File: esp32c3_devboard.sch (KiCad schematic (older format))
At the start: 0 parts

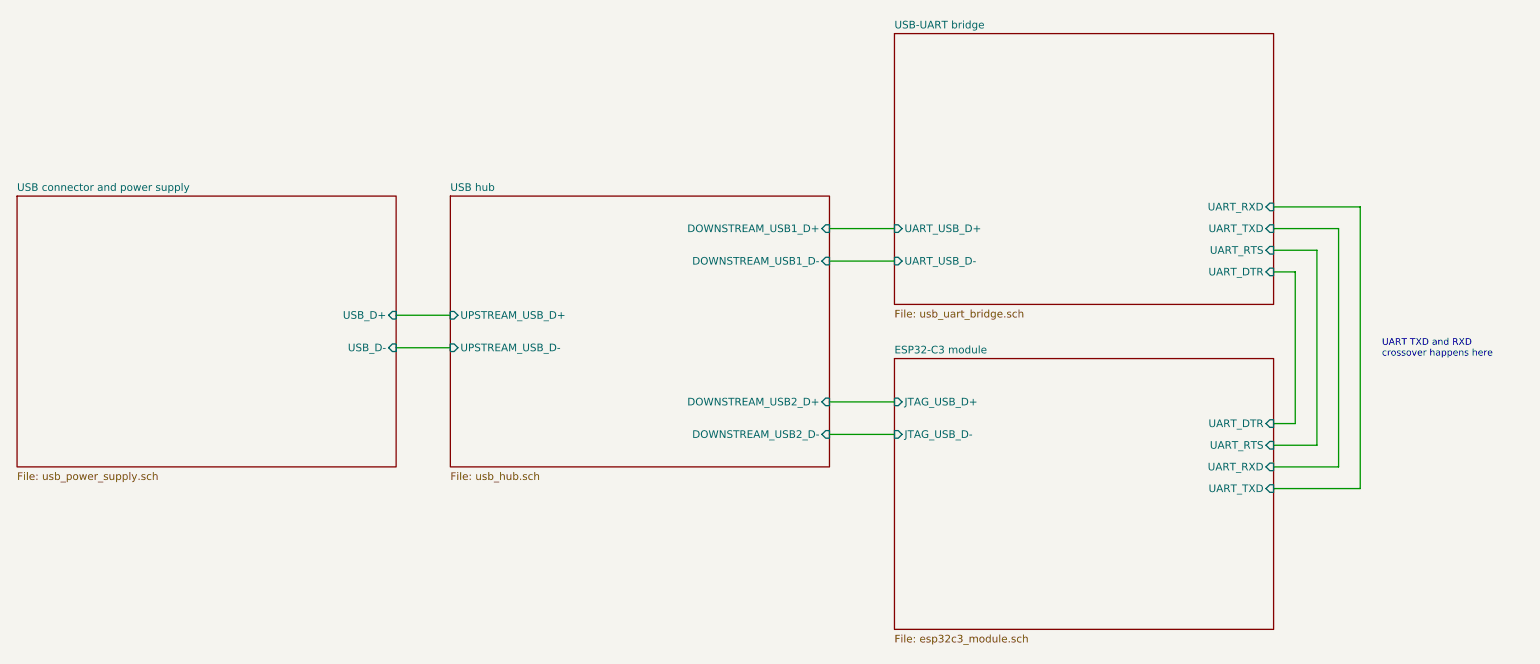
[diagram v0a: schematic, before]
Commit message: Use ESP32-C3-WROOM-02 module
Signed-off-by: Tomislav Milkovic <tomislav.milkovic95@gmail.com>
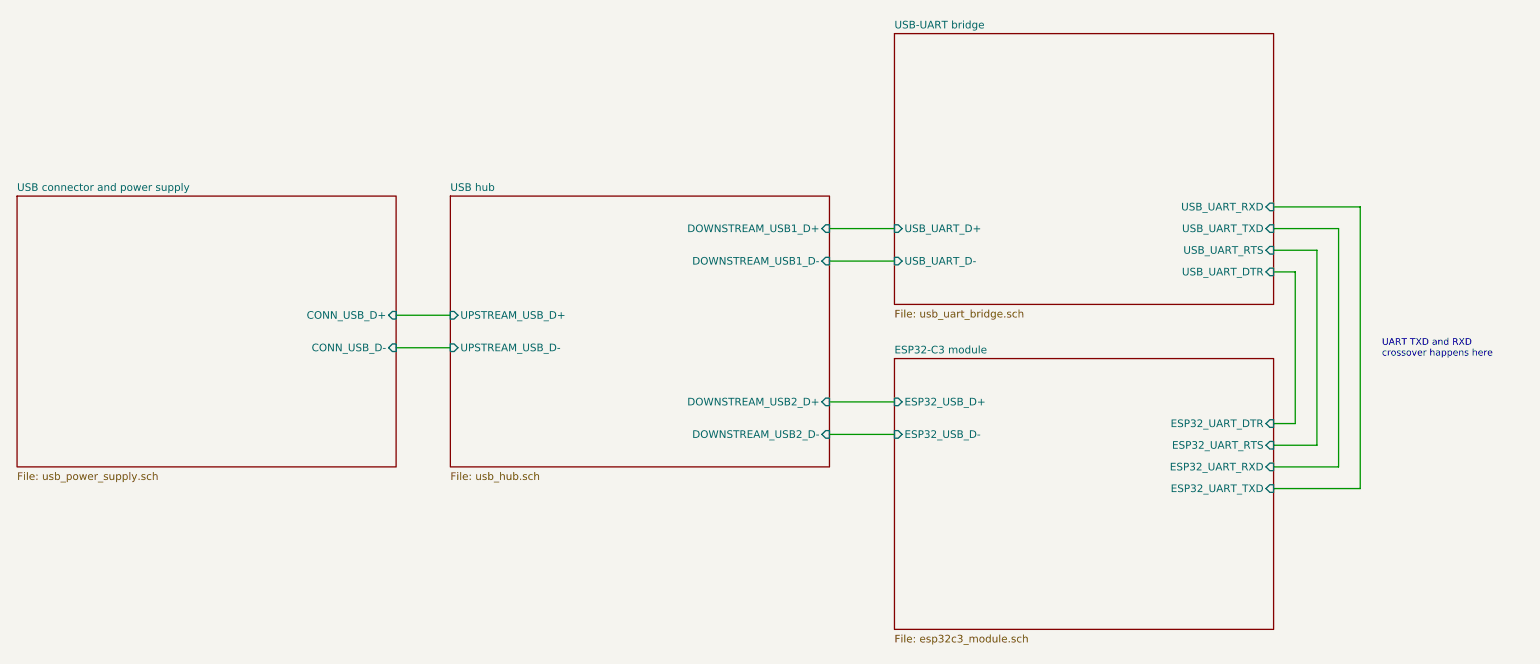
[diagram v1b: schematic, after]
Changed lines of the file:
@@
-$EndSheet
-$Sheet
-S 6700 2350 1750 1250
-U 638054C7
-F0 "USB-UART bridge" 35
-F1 "usb_uart_bridge.sch" 35
-F2 "UART_USB_D+" I L 6700 3250 35
-F3 "UART_USB_D-" I L 6700 3400 35
-F4 "UART_RTS" I R 8450 3350 35
-F5 "UART_TXD" I R 8450 3250 35
-F6 "UART_RXD" I R 8450 3150 35
-F7 "UART_DTR" I R 8450 3450 35
 $EndSheet
 $Sheet
@@
 F0 "ESP32-C3 module" 35
 F1 "esp32c3_module.sch" 35
-F2 "JTAG_USB_D+" I L 6700 4050 35
-F3 "JTAG_USB_D-" I L 6700 4200 35
-F4 "UART_RXD" I R 8450 4350 35
-F5 "UART_TXD" I R 8450 4450 35
-F6 "UART_DTR" I R 8450 4150 35
-F7 "UART_RTS" I R 8450 4250 35
+F2 "ESP32_USB_D+" I L 6700 4050 35
+F3 "ESP32_USB_D-" I L 6700 4200 35
+F4 "ESP32_UART_RXD" I R 8450 4350 35
+F5 "ESP32_UART_TXD" I R 8450 4450 35
+F6 "ESP32_UART_DTR" I R 8450 4150 35
+F7 "ESP32_UART_RTS" I R 8450 4250 35
 $EndSheet
 $Sheet
@@
 F0 "USB connector and power supply" 35
 F1 "usb_power_supply.sch" 35
-F2 "USB_D+" I R 4400 3650 35
-F3 "USB_D-" I R 4400 3800 35
+F2 "CONN_USB_D+" I R 4400 3650 35
+F3 "CONN_USB_D-" I R 4400 3800 35
 $EndSheet
 Wire Wire Line
@@
 Wire Wire Line
 	8850 4450 8450 4450
+$Sheet
+S 6700 2350 1750 1250
+U 638054C7
+F0 "USB-UART bridge" 35
+F1 "usb_uart_bridge.sch" 35
+F2 "USB_UART_D+" I L 6700 3250 35
+F3 "USB_UART_D-" I L 6700 3400 35
+F4 "USB_UART_DTR" I R 8450 3450 35
+F5 "USB_UART_RTS" I R 8450 3350 35
+F6 "USB_UART_RXD" I R 8450 3150 35
+F7 "USB_UART_TXD" I R 8450 3250 35
+$EndSheet
 $EndSCHEMATC
